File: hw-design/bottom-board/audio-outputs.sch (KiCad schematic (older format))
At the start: 56 parts, among them J10 NYS215, J9 NYS215, K1 G6S-2, K2 G6S-2, Q1 2N7002, Q2 2N7002, U11 OPA1678, U12 OPA1678

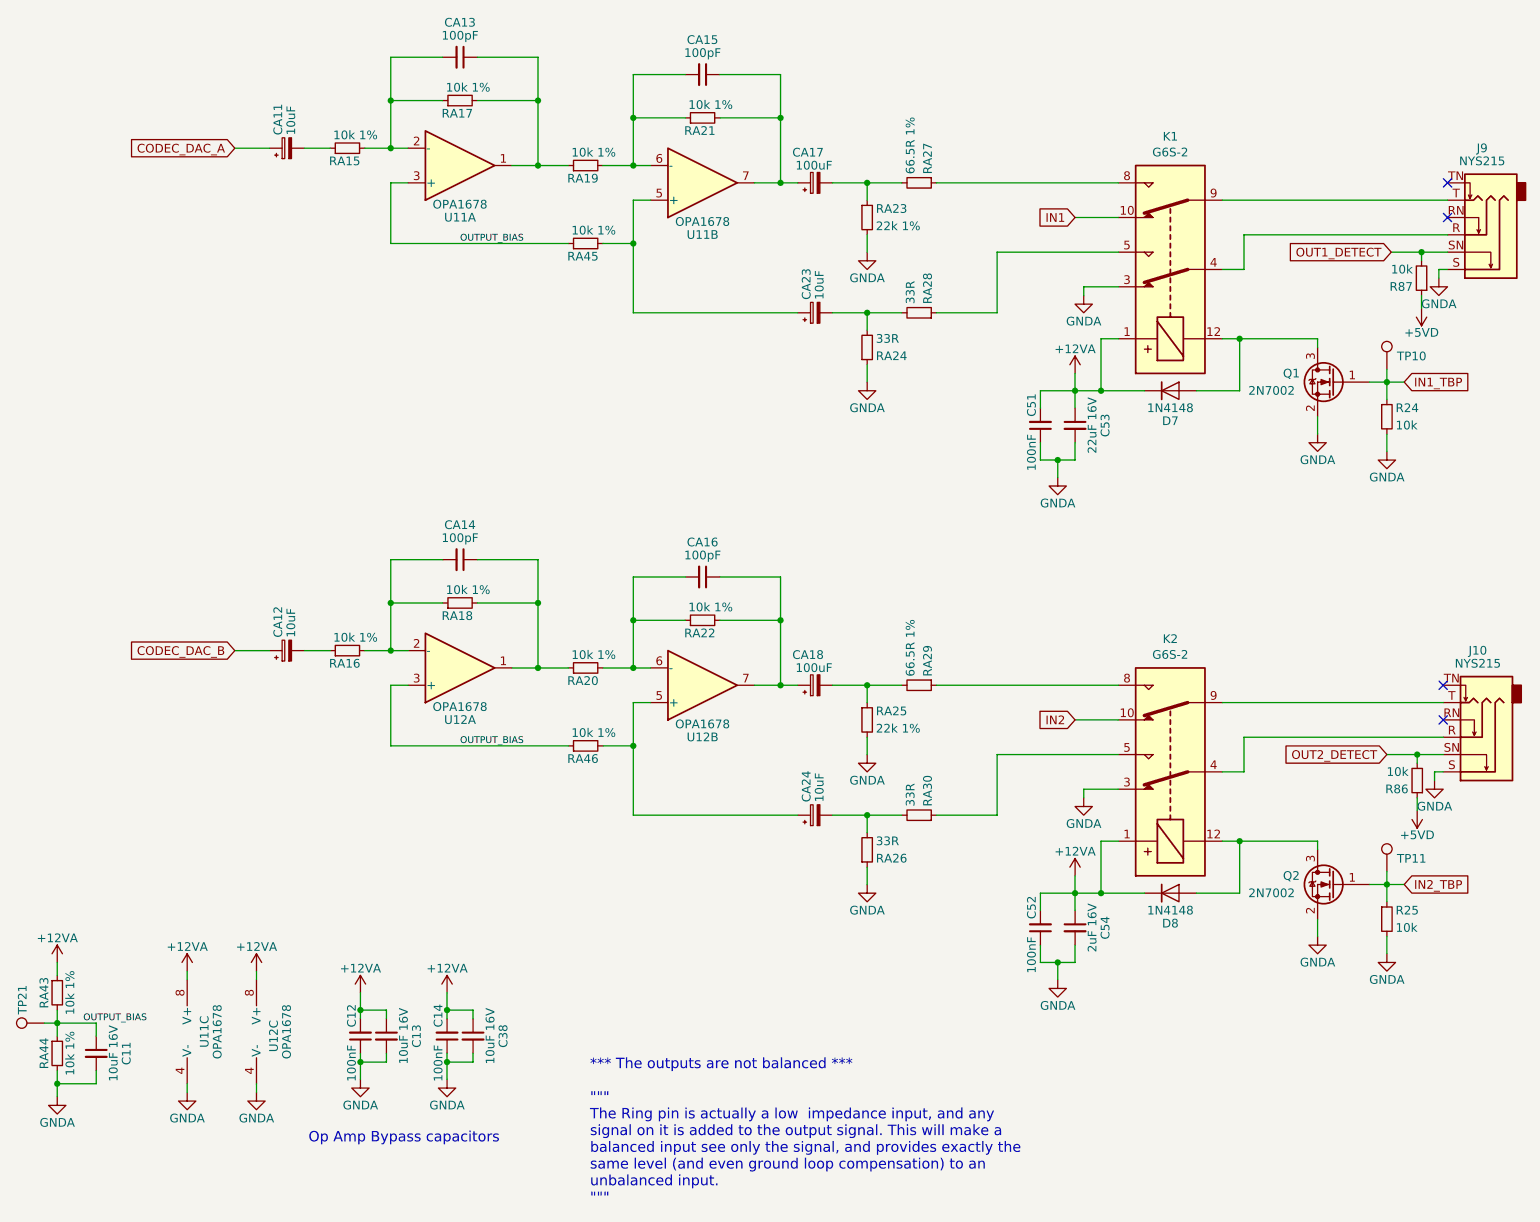
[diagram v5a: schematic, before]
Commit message: update resistor MPN's and fix design rules errors
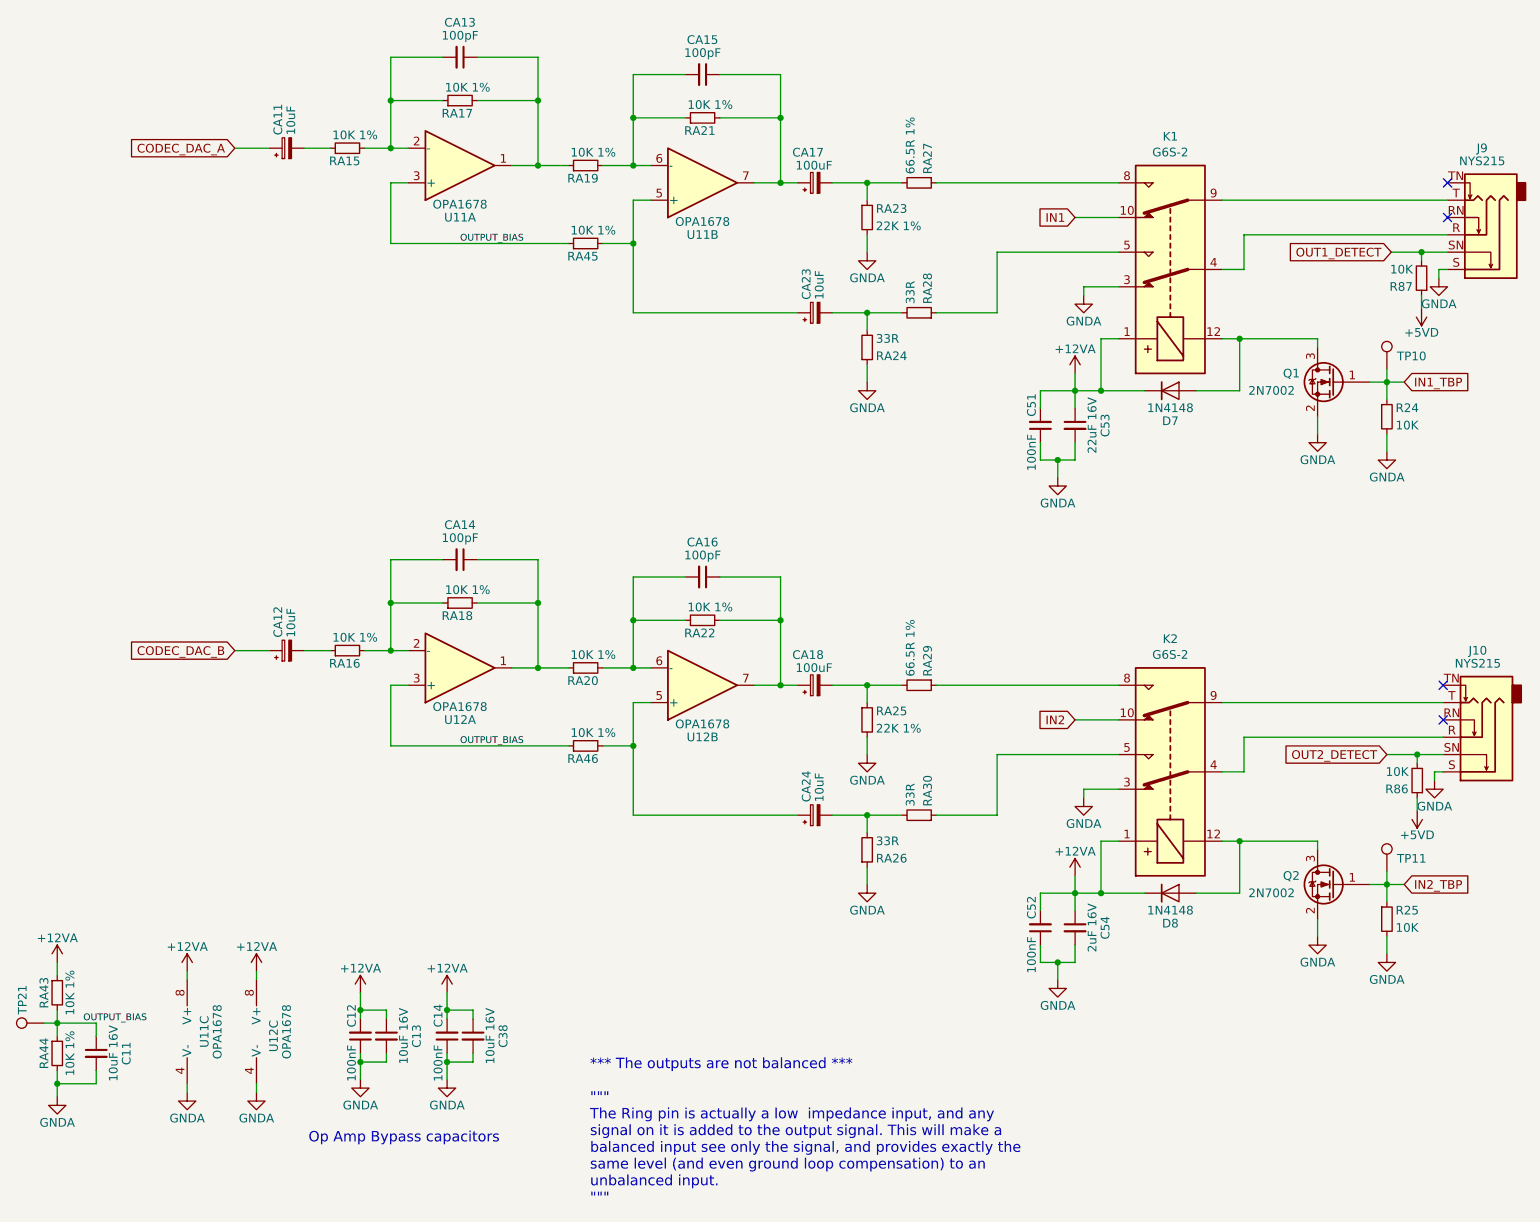
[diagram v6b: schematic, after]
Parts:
- R24, R25, R86, R87: value 10k -> 10K; MPN RMCF0603JT10K0 -> RR0816P-103-D
- RA15, RA16, RA17, RA18, RA19, RA20, RA21, RA22, RA43, RA44, RA45, RA46: value 10k 1% -> 10K 1%
- RA23, RA25: value 22k 1% -> 22K 1%
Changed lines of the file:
@@
 P 5600 1950
 F 0 "RA23" H 5650 2000 50  0000 L CNN
-F 1 "22k 1%" H 5650 1900 50  0000 L CNN
+F 1 "22K 1%" H 5650 1900 50  0000 L CNN
 F 2 "Resistor_SMD:R_0603_1608Metric" H 5600 1950 60  0001 C CNN
 F 3 "" H 5600 1950 60  0000 C CNN
@@
 AR Path="/54F72CD0/5B6BA607" Ref="RA15"  Part="1"
 F 0 "RA15" V 2525 1475 50  0000 L CNN
-F 1 "10k 1%" V 2675 1375 50  0000 L CNN
+F 1 "10K 1%" V 2675 1375 50  0000 L CNN
 F 2 "Resistor_SMD:R_0603_1608Metric" H 2600 1550 50  0001 C CNN
 F 3 "" H 2600 1550 50  0001 C CNN
@@
 AR Path="/54F72CD0/5B6C613D" Ref="RA16"  Part="1"
 F 0 "RA16" V 2525 4375 50  0000 L CNN
-F 1 "10k 1%" V 2675 4275 50  0000 L CNN
+F 1 "10K 1%" V 2675 4275 50  0000 L CNN
 F 2 "Resistor_SMD:R_0603_1608Metric" H 2600 4450 50  0001 C CNN
 F 3 "" H 2600 4450 50  0001 C CNN
@@
 AR Path="/54F72CD0/5B6C82BA" Ref="RA17"  Part="1"
 F 0 "RA17" V 3175 1200 50  0000 L CNN
-F 1 "10k 1%" V 3325 1100 50  0000 L CNN
+F 1 "10K 1%" V 3325 1100 50  0000 L CNN
 F 2 "Resistor_SMD:R_0603_1608Metric" H 3250 1275 50  0001 C CNN
 F 3 "" H 3250 1275 50  0001 C CNN
@@
 AR Path="/54F72CD0/5B6C8376" Ref="RA19"  Part="1"
 F 0 "RA19" V 3900 1575 50  0000 L CNN
-F 1 "10k 1%" V 4050 1475 50  0000 L CNN
+F 1 "10K 1%" V 4050 1475 50  0000 L CNN
 F 2 "Resistor_SMD:R_0603_1608Metric" H 3975 1650 50  0001 C CNN
 F 3 "" H 3975 1650 50  0001 C CNN
@@
 AR Path="/54F72CD0/5B6CECC1" Ref="RA20"  Part="1"
 F 0 "RA20" V 3900 4475 50  0000 L CNN
-F 1 "10k 1%" V 4050 4375 50  0000 L CNN
+F 1 "10K 1%" V 4050 4375 50  0000 L CNN
 F 2 "Resistor_SMD:R_0603_1608Metric" H 3975 4550 50  0001 C CNN
 F 3 "" H 3975 4550 50  0001 C CNN
@@
 P 5600 4850
 F 0 "RA25" H 5650 4900 50  0000 L CNN
-F 1 "22k 1%" H 5650 4800 50  0000 L CNN
+F 1 "22K 1%" H 5650 4800 50  0000 L CNN
 F 2 "Resistor_SMD:R_0603_1608Metric" H 5600 4850 60  0001 C CNN
 F 3 "" H 5600 4850 60  0000 C CNN
@@
 AR Path="/54F72CD0/5B91B0E5" Ref="RA21"  Part="1"
 F 0 "RA21" V 4575 1300 50  0000 L CNN
-F 1 "10k 1%" V 4725 1200 50  0000 L CNN
+F 1 "10K 1%" V 4725 1200 50  0000 L CNN
 F 2 "Resistor_SMD:R_0603_1608Metric" H 4650 1375 50  0001 C CNN
 F 3 "" H 4650 1375 50  0001 C CNN
@@
 AR Path="/54F72CD0/5B9340F2" Ref="RA18"  Part="1"
 F 0 "RA18" V 3175 4100 50  0000 L CNN
-F 1 "10k 1%" V 3325 4000 50  0000 L CNN
+F 1 "10K 1%" V 3325 4000 50  0000 L CNN
 F 2 "Resistor_SMD:R_0603_1608Metric" H 3250 4175 50  0001 C CNN
 F 3 "" H 3250 4175 50  0001 C CNN
@@
 AR Path="/54F72CD0/5B93D682" Ref="RA22"  Part="1"
 F 0 "RA22" V 4575 4200 50  0000 L CNN
-F 1 "10k 1%" V 4725 4100 50  0000 L CNN
+F 1 "10K 1%" V 4725 4100 50  0000 L CNN
 F 2 "Resistor_SMD:R_0603_1608Metric" H 4650 4275 50  0001 C CNN
 F 3 "" H 4650 4275 50  0001 C CNN
@@
 AR Path="/54F72CD0/5B949CDF" Ref="R24"  Part="1"
 F 0 "R24" H 8650 3150 50  0000 L CNN
-F 1 "10k" H 8650 3050 50  0000 L CNN
+F 1 "10K" H 8650 3050 50  0000 L CNN
 F 2 "Resistor_SMD:R_0603_1608Metric" H 8600 3100 60  0001 C CNN
 F 3 "" H 8600 3100 60  0000 C CNN
-F 4 "RMCF0603JT10K0" H 6850 -3550 50  0001 C CNN "MPN"
+F 4 "RR0816P-103-D" H 6850 -3550 50  0001 C CNN "MPN"
 	1    8600 3100
 	1    0    0    -1
@@
 AR Path="/54F72CD0/5B953464" Ref="R25"  Part="1"
 F 0 "R25" H 8650 6050 50  0000 L CNN
-F 1 "10k" H 8650 5950 50  0000 L CNN
+F 1 "10K" H 8650 5950 50  0000 L CNN
 F 2 "Resistor_SMD:R_0603_1608Metric" H 8600 6000 60  0001 C CNN
 F 3 "" H 8600 6000 60  0000 C CNN
-F 4 "RMCF0603JT10K0" H 6850 -650 50  0001 C CNN "MPN"
+F 4 "RR0816P-103-D" H 6850 -650 50  0001 C CNN "MPN"
 	1    8600 6000
 	1    0    0    -1
@@
 AR Path="/54F72CD0/5BD4AC71" Ref="RA43"  Part="1"
 F 0 "RA43" V 850 6425 50  0000 C CNN
-F 1 "10k 1%" V 1000 6425 50  0000 C CNN
+F 1 "10K 1%" V 1000 6425 50  0000 C CNN
 F 2 "Resistor_SMD:R_0603_1608Metric" H 925 6425 50  0001 C CNN
 F 3 "" H 925 6425 50  0001 C CNN
@@
 AR Path="/54F72CD0/5BD4AC7B" Ref="RA44"  Part="1"
 F 0 "RA44" V 850 6775 50  0000 C CNN
-F 1 "10k 1%" V 1000 6775 50  0000 C CNN
+F 1 "10K 1%" V 1000 6775 50  0000 C CNN
 F 2 "Resistor_SMD:R_0603_1608Metric" H 925 6775 50  0001 C CNN
 F 3 "" H 925 6775 50  0001 C CNN
@@
 AR Path="/54F72CD0/5BE71C75" Ref="RA45"  Part="1"
 F 0 "RA45" V 3900 2025 50  0000 L CNN
-F 1 "10k 1%" V 4050 1925 50  0000 L CNN
+F 1 "10K 1%" V 4050 1925 50  0000 L CNN
 F 2 "Resistor_SMD:R_0603_1608Metric" H 3975 2100 50  0001 C CNN
 F 3 "" H 3975 2100 50  0001 C CNN
@@
 AR Path="/54F72CD0/5BEB2CC5" Ref="RA46"  Part="1"
 F 0 "RA46" V 3900 4925 50  0000 L CNN
-F 1 "10k 1%" V 4050 4825 50  0000 L CNN
+F 1 "10K 1%" V 4050 4825 50  0000 L CNN
 F 2 "Resistor_SMD:R_0603_1608Metric" H 3975 5000 50  0001 C CNN
 F 3 "" H 3975 5000 50  0001 C CNN
@@
 AR Path="/54F72CD0/5DF9BAE3" Ref="R87"  Part="1"
 F 0 "R87" H 8850 2350 50  0000 L CNN
-F 1 "10k" H 8850 2250 50  0000 L CNN
+F 1 "10K" H 8850 2250 50  0000 L CNN
 F 2 "Resistor_SMD:R_0603_1608Metric" H 8800 2300 60  0001 C CNN
 F 3 "" H 8800 2300 60  0000 C CNN
-F 4 "RMCF0603JT10K0" H 2050 -675 50  0001 C CNN "MPN"
+F 4 "RR0816P-103-D" H 2050 -675 50  0001 C CNN "MPN"
 	1    8800 2300
 	-1   0    0    1
@@
 AR Path="/54F72CD0/5E033F13" Ref="R86"  Part="1"
 F 0 "R86" H 8825 5250 50  0000 L CNN
-F 1 "10k" H 8825 5150 50  0000 L CNN
+F 1 "10K" H 8825 5150 50  0000 L CNN
 F 2 "Resistor_SMD:R_0603_1608Metric" H 8775 5200 60  0001 C CNN
 F 3 "" H 8775 5200 60  0000 C CNN
-F 4 "RMCF0603JT10K0" H 2025 2225 50  0001 C CNN "MPN"
+F 4 "RR0816P-103-D" H 2025 2225 50  0001 C CNN "MPN"
 	1    8775 5200
 	-1   0    0    1
